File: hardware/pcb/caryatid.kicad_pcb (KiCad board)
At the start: 2 copper layers, 150 x 90 mm, 129 parts, among them J1 DC in, J10 FSR, J11 Digital bus, J12 RGB status, J13A Comms A - Qwiic, J13B Comms A - module, J14 Mic bias return, J15 Comms B - module, J16 Expansion / SPI1, J17 Audio out L/R/G, J18 Audio in L/R/rtn, J2 Battery, remote, J3 Latch switch, J4 Charge LEDs, J5 Analogue bus, J6 SW1 switch, J7 SW2 switch, J8 SW3 switch, J9 Soft pot, U1 BQ24074RGT, U2 TPS61023DRL, U3 74HC14, U4 MCP6002

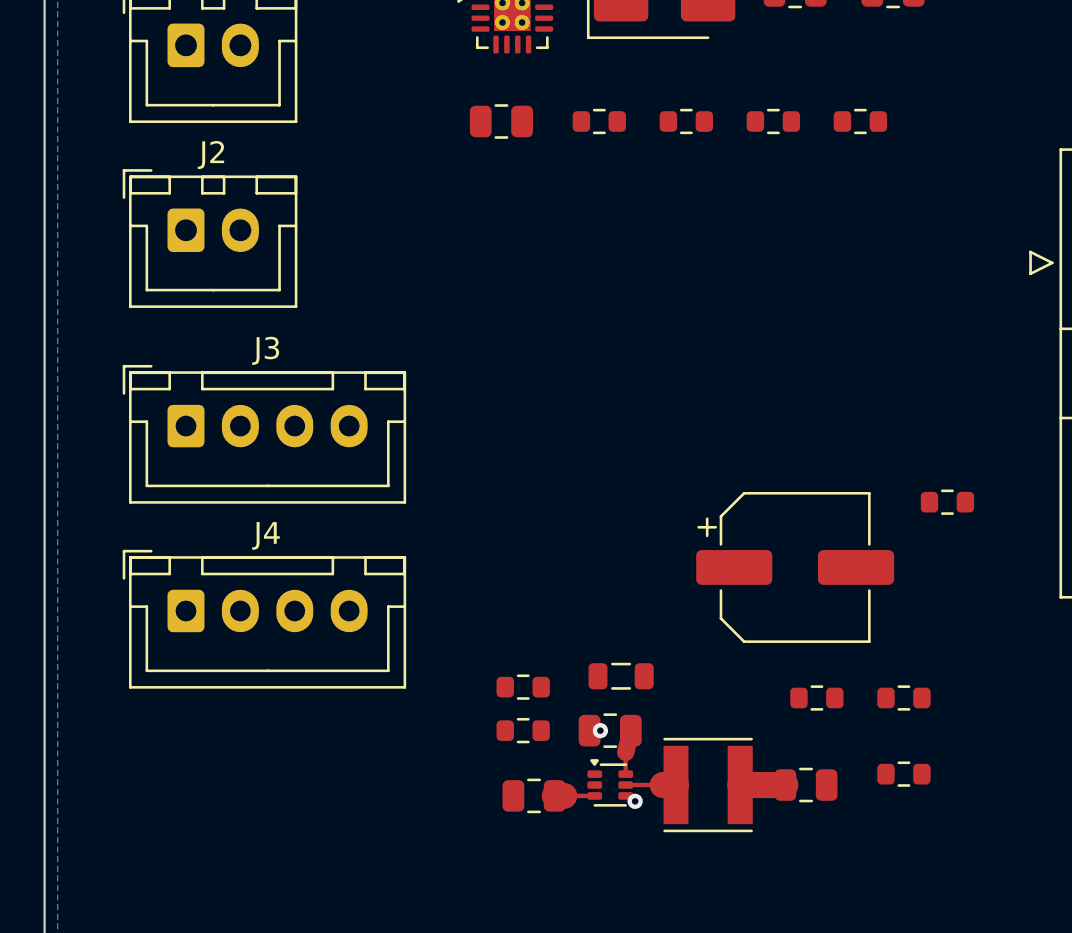
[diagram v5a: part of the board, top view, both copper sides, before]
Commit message: Remove J2, the remote-pack connector
Nothing on the platform asked for it, and it was the last route by which a
reversed cell could reach the charger. BAT is rated -0.3 V to 5 V against a
reversed cell's -4.2 V, and there is deliberately no reverse protection because
a soldered holder cannot be wired backwards. J2 was the one exception -- a
hand-crimped loom on a keyed connector that can still be crimped wrong. With it
gone the exposure is not mitigated, it is absent: no connector on the board
reaches VBAT.

Removed surgically from power.kicad_sch by the generator's deterministic UUIDs --
symbol, both wire stubs, both power symbols -- rather than by re-running the
one-shot, which would have discarded anything done in the GUI since.

124 components, VBAT down to BT1.1, C2.1, R11.1, U1.2, U1.3.

Two things this shook out. Editing the VBAT symbol's description in one sheet's
embedded lib_symbols made it disagree with the library and with the other sheets,
which ERC reported as five lib_symbol_mismatch warnings; every sheet carries its
own copy and all of them need the same edit. And place_board.py's collision check
still split parts by is_smd(), which stopped meaning front/back when everything
moved to one face -- it has been collapsed to a single group, with
tools/check_board.py remaining the authority since it reads the board itself.

ERC 0. DRC non-ratsnest 9. All eight checks pass. Pin map unchanged.
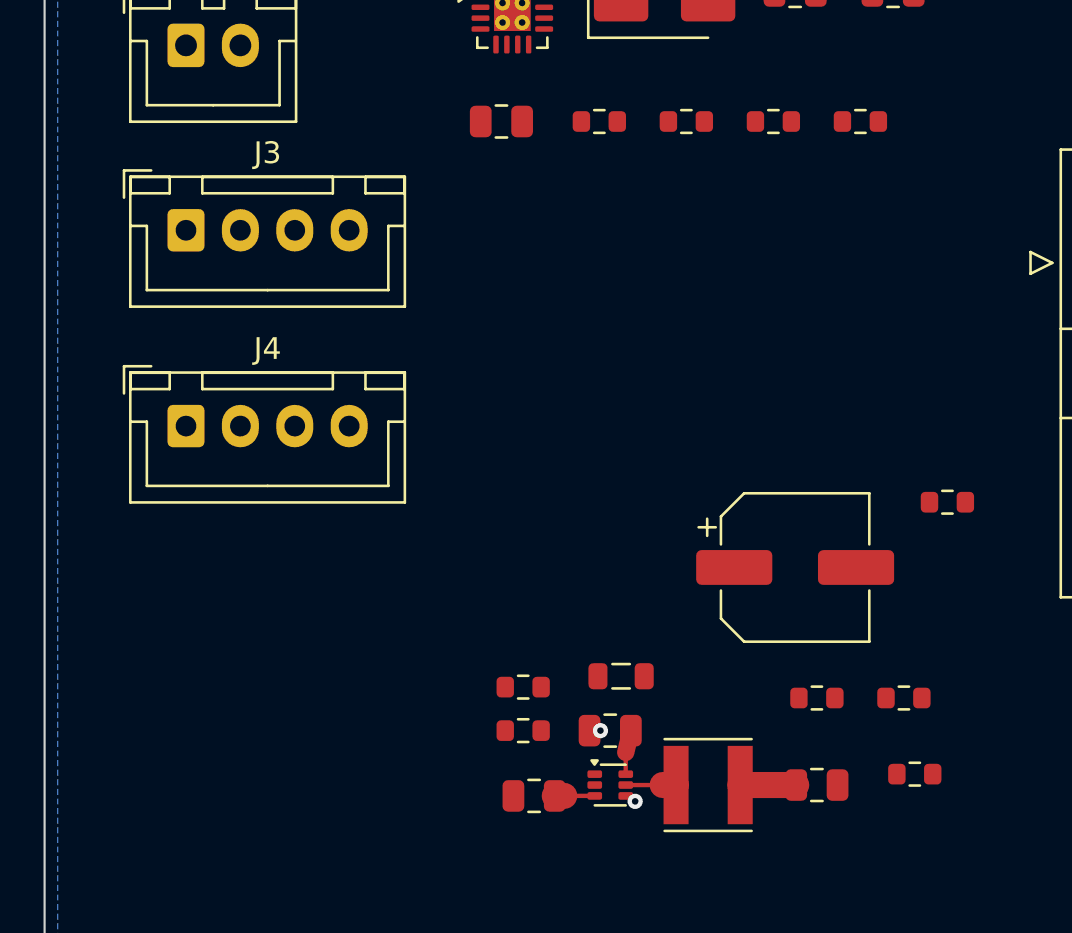
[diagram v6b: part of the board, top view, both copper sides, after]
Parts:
- removed J2: Battery, remote, Connector_JST:JST_XH_B2B-XH-A_1x02_P2.50mm_Vertical
- moved J3 9.00 mm to (56.5, 70.5)
- moved J4 8.50 mm to (56.5, 79.5)
- moved C5 0.50 mm to (85.5, 96.0)
- moved R10 0.50 mm to (90.0, 95.5)
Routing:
- net VOUT: track 3.91 -> 4.41 mm

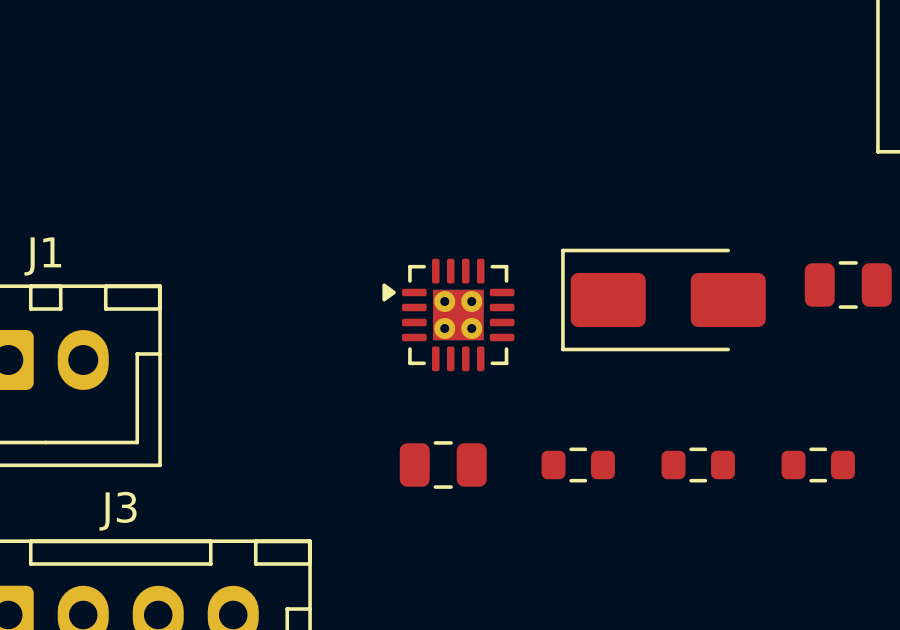
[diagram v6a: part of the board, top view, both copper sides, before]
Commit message: Fan out U1's six power pads so the router can reach them
Freerouting routes a net at one width -- its class width -- and has no
neck-down. A HighCurrent net at 1.20 mm therefore cannot leave U1's 0.25 mm
QFN pads on 0.5 mm pitch, and the router simply failed those connections:
eleven of the thirteen unrouted in the last run were at U1 or U2.

tools/fanout.py escapes each such pad at a width that fits between its
neighbours, runs out until the package stops constraining anything, widens to
the class width, and leaves the result for export_dsn.py to mark protected.
Six escapes, all at U1:

  U1-2, U1-3    VBAT     0.30 mm neck, 1.10 mm, then 1.20
  U1-5,10,11    VOUT     0.30 mm neck, 1.10-1.15, then 1.20
  U1-13         VIN_DC   0.30 mm neck, 1.10 mm, then 1.20

KiCad DRC reports no clearance violation from any of it. The count goes 9 to
11 and both new items are track_dangling -- the stub ends, waiting for the
router, which is what an unrouted fanout should look like.

Three things the tool models that hand-measuring got wrong, all the same
shape as the rest of this board's history -- a check that captures one thing
and quietly ignores another:

  * "track wider than the pad" is not the criterion. Clearance to the
    NEIGHBOUR is. Seven pads turn out to take the class width directly and
    need no neck; necking them would be clutter and two extra joints.
  * measuring the widest track that fits SYMMETRICALLY about the pad centre
    reported 0.070 mm at U1, below JLC's floor -- i.e. no legal escape. That
    was nonsense: the nearest neighbour it found was U1-17, the exposed pad,
    which sits BEHIND the pins. An escape runs outward. A swept trace has a
    direction; a disc does not.
  * U1 and U2 carry a footprint-level (clearance 0.15) override, added
    deliberately because HighCurrent's 0.30 is stricter than a 0.5 mm-pitch
    QFN allows. Applying the netclass everywhere declared four escapes
    impossible that the board's own rules permit. It is written a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
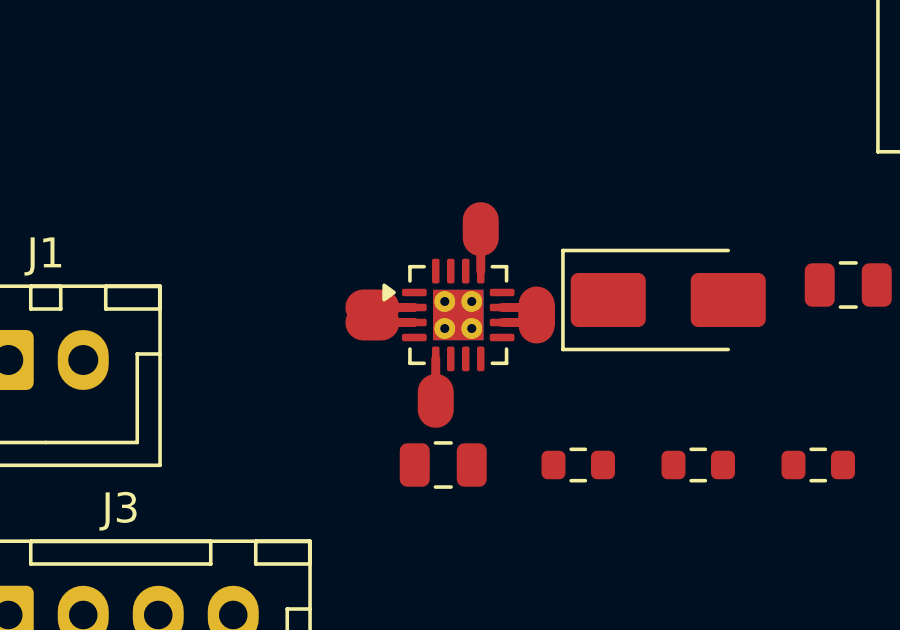
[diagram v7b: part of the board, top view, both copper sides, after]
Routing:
- net VOUT: track 4.41 -> 9.61 mm
- net VBAT: track 0.00 -> 3.40 mm
- net VIN_DC: track 0.00 -> 1.70 mm
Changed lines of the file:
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@@
 		)
 	)
+	(segment
+		(start 72.9625 60.7500)
+		(end 74.1125 60.7500)
+		(width 0.3)
+		(layer "F.Cu")
+		(net 94)
+	)
+	(segment
+		(start 74.1125 60.7500)
+		(end 74.1125 60.1500)
+		(width 1.2)
+		(layer "F.Cu")
+		(net 94)
+	)
+	(segment
+		(start 72.9625 60.2500)
+		(end 74.1125 60.2500)
+		(width 0.3)
+		(layer "F.Cu")
+		(net 94)
+	)
+	(segment
+		(start 74.1125 60.2500)
+		(end 74.1125 60.8500)
+		(width 1.2)
+		(layer "F.Cu")
+		(net 94)
+	)
+	(segment
+		(start 72.2500 59.0375)
+		(end 72.2500 57.9375)
+		(width 0.3)
+		(layer "F.Cu")
+		(net 93)
+	)
+	(segment
+		(start 72.2500 57.9375)
+		(end 72.2500 57.3375)
+		(width 1.2)
+		(layer "F.Cu")
+		(net 93)
+	)
+	(segment
+		(start 70.0375 60.2500)
+		(end 68.9375 60.2500)
+		(width 0.3)
+		(layer "F.Cu")
+		(net 92)
+	)
+	(segment
+		(start 68.9375 60.2500)
+		(end 68.3375 60.2500)
+		(width 1.2)
+		(layer "F.Cu")
+		(net 92)
+	)
+	(segment
+		(start 70.0375 60.7500)
+		(end 68.9375 60.7500)
+		(width 0.3)
+		(layer "F.Cu")
+		(net 92)
+	)
+	(segment
+		(start 68.9375 60.7500)
+		(end 68.3375 60.7500)
+		(width 1.2)
+		(layer "F.Cu")
+		(net 92)
+	)
+	(segment
+		(start 70.7500 61.9625)
+		(end 70.7500 63.0625)
+		(width 0.3)
+		(layer "F.Cu")
+		(net 94)
+	)
+	(segment
+		(start 70.7500 63.0625)
+		(end 70.7500 63.6625)
+		(width 1.2)
+		(layer "F.Cu")
+		(net 94)
+	)
 )

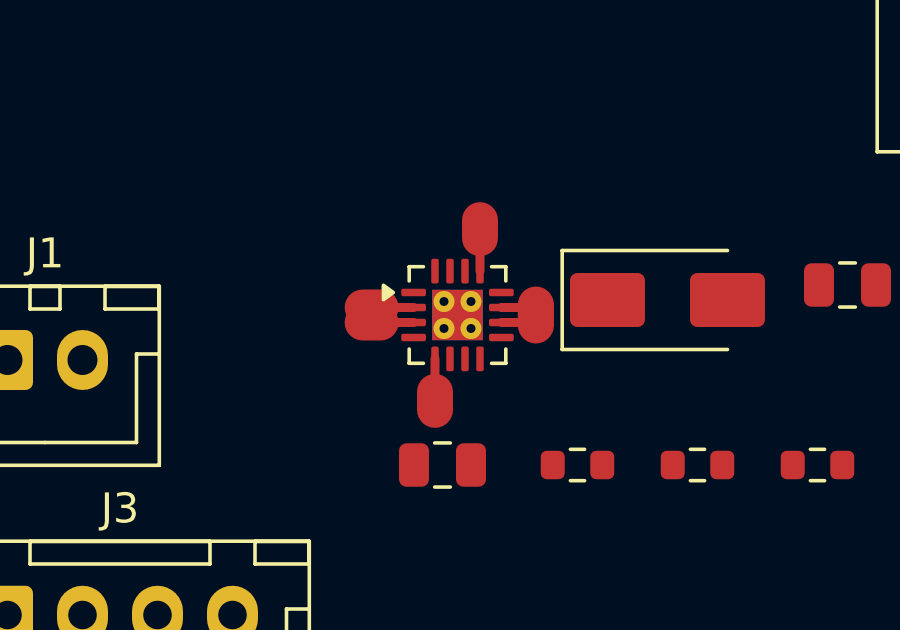
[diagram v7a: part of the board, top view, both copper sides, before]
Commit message: Tie U1's paired power pads and escape each group once
Replaces the per-pad fanout in 0722688, which made routing WORSE: 15 unrouted
and 141 violations against 13 and 127 before it, and 2826 seconds against 163.

The reason was not the idea but the greed. Each escape took the widest neck
that fit when considered ALONE, and 0.30 mm per pad ate the gap the signal
pins beside them needed. Measured after the fact, U1-1, U1-9, U1-12 and U1-14
were left 0.025 mm of working room, against 0.100 mm for pads no escape sat
beside. Legal by DRC, unusable by a router -- and /power/TS, /power/ILIM and
/power/TMR duly stopped routing, having been fine before.

Three changes:

  * VBAT is on U1-2 AND U1-3, VOUT on U1-10 AND U1-11. Tie each pair with a
    0.20 mm link and escape the pair ONCE from its midpoint. That puts the
    escape a full pitch from the nearest other-net pad instead of half a
    pitch, so it is both wider and less intrusive than two parallel escapes
    fighting for the same gap.
  * Take the NARROWEST adequate escape, not the widest that fits. The neck
    only has to carry what the pads themselves provide -- it is about a
    millimetre long between a pad and a plane, and the pad is the real
    constriction -- so the target is pad width x pads feeding it. 0.50 mm for
    a tied pair, 0.25 mm for a singleton. Anything past that is room taken
    from a neighbour that also has to get out.
  * Check the neighbours, and refuse if they are squeezed. Every escape in
    0722688 was verified against the board as it stood and every one passed;
    none was checked against the pins that still had to get out PAST it. The
    tool now treats its own proposals as copper and confirms every remaining
    pad on the package can still leave at its class width with 0.05 mm to
    spare, retrying with the widening pushed further off the pad row until
    that holds. It refuses to write rather than ship a legal-but-unroutable
    board.

Result: minimum neighbour slack doubles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
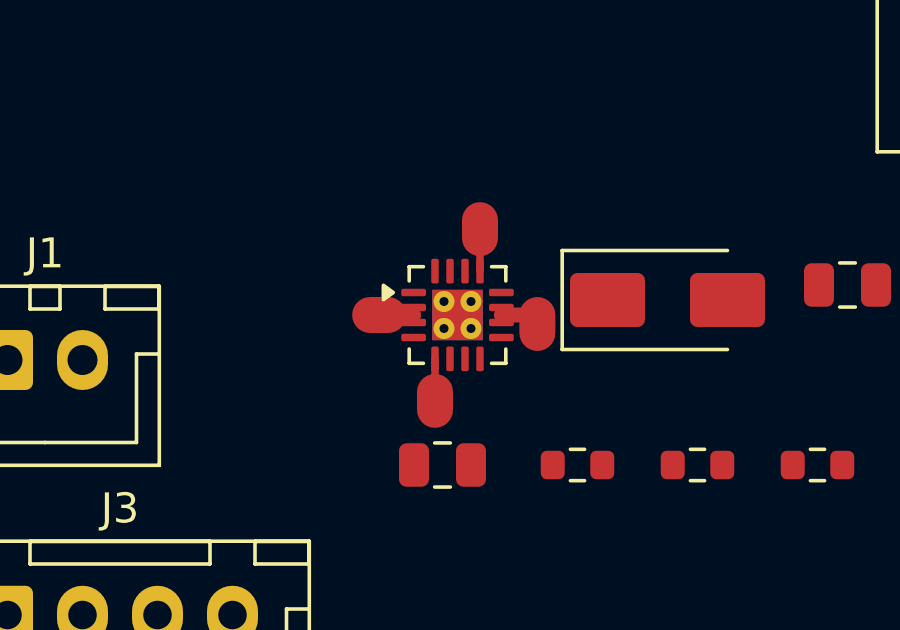
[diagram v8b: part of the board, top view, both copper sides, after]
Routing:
- net VBAT: track 3.40 -> 1.95 mm
- net VOUT: track 9.61 -> 8.41 mm
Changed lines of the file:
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@@
 	)
 	(segment
-		(start 72.9625 60.7500)
-		(end 74.1125 60.7500)
-		(width 0.3)
+		(start 70.0375 60.2500)
+		(end 70.0375 60.7500)
+		(width 0.2)
+		(layer "F.Cu")
+		(net 92)
+	)
+	(segment
+		(start 70.0375 60.5000)
+		(end 69.1875 60.5000)
+		(width 0.5)
+		(layer "F.Cu")
+		(net 92)
+	)
+	(segment
+		(start 69.1875 60.5000)
+		(end 68.5875 60.5000)
+		(width 1.2)
+		(layer "F.Cu")
+		(net 92)
+	)
+	(segment
+		(start 70.7500 61.9625)
+		(end 70.7500 63.0625)
+		(width 0.25)
 		(layer "F.Cu")
 		(net 94)
 	)
 	(segment
-		(start 74.1125 60.7500)
-		(end 74.1125 60.1500)
+		(start 70.7500 63.0625)
+		(end 70.7500 63.6625)
 		(width 1.2)
 		(layer "F.Cu")
@@
 	(segment
 		(start 72.9625 60.2500)
-		(end 74.1125 60.2500)
-		(width 0.3)
+		(end 72.9625 60.7500)
+		(width 0.2)
 		(layer "F.Cu")
 		(net 94)
 	)
 	(segment
-		(start 74.1125 60.2500)
-		(end 74.1125 60.8500)
+		(start 72.9625 60.5000)
+		(end 74.1625 60.5000)
+		(width 0.5)
+		(layer "F.Cu")
+		(net 94)
+	)
+	(segment
+		(start 74.1625 60.5000)
+		(end 74.1625 61.1000)
 		(width 1.2)
 		(layer "F.Cu")
@@
 		(start 72.2500 59.0375)
 		(end 72.2500 57.9375)
-		(width 0.3)
+		(width 0.25)
 		(layer "F.Cu")
 		(net 93)
@@
 		(net 93)
 	)
-	(segment
-		(start 70.0375 60.2500)
-		(end 68.9375 60.2500)
-		(width 0.3)
-		(layer "F.Cu")
-		(net 92)
-	)
-	(segment
-		(start 68.9375 60.2500)
-		(end 68.3375 60.2500)
-		(width 1.2)
-		(layer "F.Cu")
-		(net 92)
-	)
-	(segment
-		(start 70.0375 60.7500)
-		(end 68.9375 60.7500)
-		(width 0.3)
-		(layer "F.Cu")
-		(net 92)
-	)
-	(segment
-		(start 68.9375 60.7500)
-		(end 68.3375 60.7500)
-		(width 1.2)
-		(layer "F.Cu")
-		(net 92)
-	)
-	(segment
-		(start 70.7500 61.9625)
-		(end 70.7500 63.0625)
-		(width 0.3)
-		(layer "F.Cu")
-		(net 94)
-	)
-	(segment
-		(start 70.7500 63.0625)
-		(end 70.7500 63.6625)
-		(width 1.2)
-		(layer "F.Cu")
-		(net 94)
-	)
 )
